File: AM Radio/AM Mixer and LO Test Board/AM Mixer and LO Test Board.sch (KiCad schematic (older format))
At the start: 47 parts, among them J1 RF_IN, J2 IF_FILT_OUT, J3 IF_PREFILT_OUT, J4 RF_IN, Q1 2N2222, Q2 2N2222, Q3 2N2222, T1 SWB2010-1-SM, T2 SWB2010-1-SM, U1 AD711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

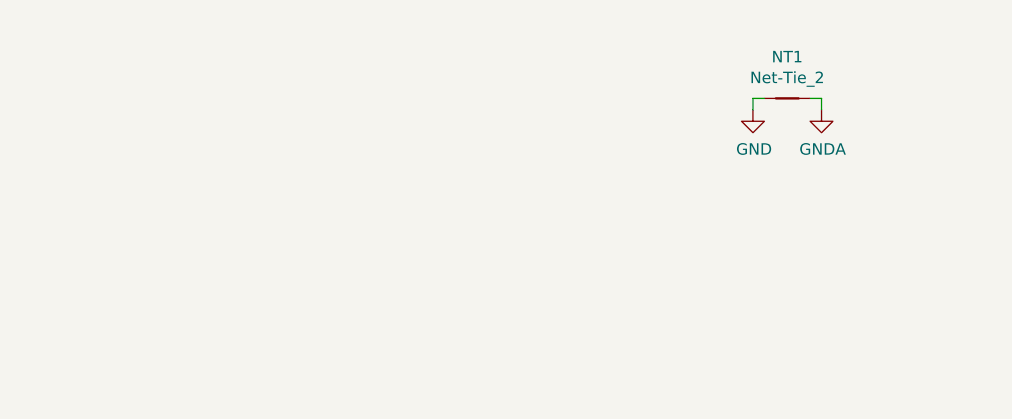
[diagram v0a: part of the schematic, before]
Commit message: Added components to PCB and set up DRC + board outline
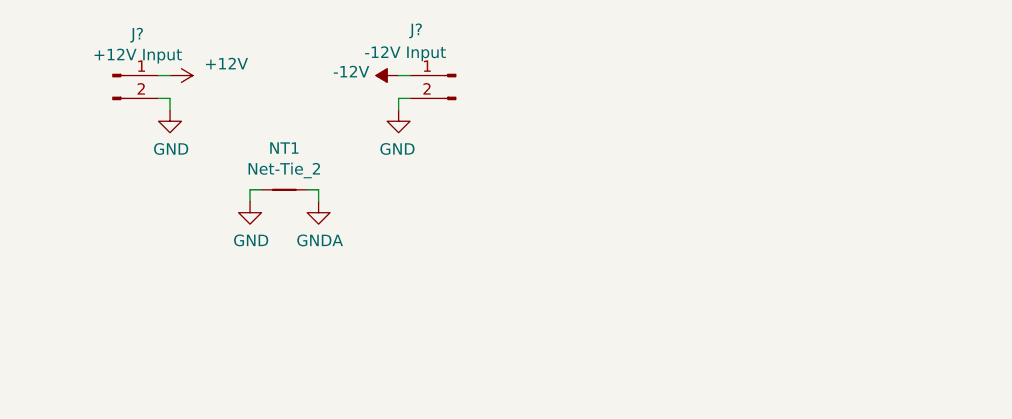
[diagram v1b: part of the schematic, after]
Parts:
- added J?: +12V Input, Connector_PinHeader_2.54mm:PinHeader_1x02_P2.54mm_Vertical, symbol Connector:Conn_01x02_Male
- added J?: -12V Input, Connector_PinHeader_2.54mm:PinHeader_1x02_P2.54mm_Vertical, symbol Connector:Conn_01x02_Male
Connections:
- net +12V: now also J?.1 (Pin_1)
- net -12V: now also J?.1 (Pin_1)
- net GND: now also J?.2 (Pin_2), J?.2 (Pin_2)
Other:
- moved on the sheet: NT1
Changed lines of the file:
@@
 L Device:Net-Tie_2 NT1
 U 1 1 60F78CC0
-P 3900 1100
-F 0 "NT1" H 3900 1281 50  0000 C CNN
-F 1 "Net-Tie_2" H 3900 1190 50  0000 C CNN
-F 2 "NetTie:NetTie-2_SMD_Pad0.5mm" H 3900 1100 50  0001 C CNN
-F 3 "~" H 3900 1100 50  0001 C CNN
-	1    3900 1100
+P 1700 1500
+F 0 "NT1" H 1700 1681 50  0000 C CNN
+F 1 "Net-Tie_2" H 1700 1590 50  0000 C CNN
+F 2 "NetTie:NetTie-2_SMD_Pad0.5mm" H 1700 1500 50  0001 C CNN
+F 3 "~" H 1700 1500 50  0001 C CNN
+	1    1700 1500
 	1    0    0    -1
 $EndComp
@@
 L power:GND #PWR032
 U 1 1 60F79A9F
-P 3750 1150
-F 0 "#PWR032" H 3750 900 50  0001 C CNN
-F 1 "GND" H 3755 977 50  0000 C CNN
-F 2 "" H 3750 1150 50  0001 C CNN
-F 3 "" H 3750 1150 50  0001 C CNN
-	1    3750 1150
+P 1550 1550
+F 0 "#PWR032" H 1550 1300 50  0001 C CNN
+F 1 "GND" H 1555 1377 50  0000 C CNN
+F 2 "" H 1550 1550 50  0001 C CNN
+F 3 "" H 1550 1550 50  0001 C CNN
+	1    1550 1550
 	1    0    0    -1
 $EndComp
 Wire Wire Line
-	3750 1150 3750 1100
+	1550 1550 1550 1500
 Wire Wire Line
-	3750 1100 3800 1100
+	1550 1500 1600 1500
 $Comp
 L power:GNDA #PWR033
 U 1 1 60F81BDB
-P 4050 1150
-F 0 "#PWR033" H 4050 900 50  0001 C CNN
-F 1 "GNDA" H 4055 977 50  0000 C CNN
-F 2 "" H 4050 1150 50  0001 C CNN
-F 3 "" H 4050 1150 50  0001 C CNN
-	1    4050 1150
+P 1850 1550
+F 0 "#PWR033" H 1850 1300 50  0001 C CNN
+F 1 "GNDA" H 1855 1377 50  0000 C CNN
+F 2 "" H 1850 1550 50  0001 C CNN
+F 3 "" H 1850 1550 50  0001 C CNN
+	1    1850 1550
 	1    0    0    -1
 $EndComp
 Wire Wire Line
-	4050 1150 4050 1100
+	1850 1550 1850 1500
 Wire Wire Line
-	4050 1100 4000 1100
+	1850 1500 1800 1500
+$Comp
+L power:+12V #PWR?
+U 1 1 60F9D5C7
+P 1200 1000
+F 0 "#PWR?" H 1200 850 50  0001 C CNN
+F 1 "+12V" V 1150 1150 50  0000 L CNN
+F 2 "" H 1200 1000 50  0001 C CNN
+F 3 "" H 1200 1000 50  0001 C CNN
+	1    1200 1000
+	0    1    1    0
+$EndComp
+Wire Wire Line
+	1150 1000 1200 1000
+$Comp
+L Connector:Conn_01x02_Male J?
+U 1 1 60FA60E9
+P 950 1000
+F 0 "J?" H 1058 1181 50  0000 C CNN
+F 1 "+12V Input" H 1058 1090 50  0000 C CNN
+F 2 "Connector_PinHeader_2.54mm:PinHeader_1x02_P2.54mm_Vertical" H 950 1000 50  0001 C CNN
+F 3 "~" H 950 1000 50  0001 C CNN
+	1    950  1000
+	1    0    0    -1
+$EndComp
+$Comp
+L power:GND #PWR?
+U 1 1 60FA6D03
+P 1200 1150
+F 0 "#PWR?" H 1200 900 50  0001 C CNN
+F 1 "GND" H 1205 977 50  0000 C CNN
+F 2 "" H 1200 1150 50  0001 C CNN
+F 3 "" H 1200 1150 50  0001 C CNN
+	1    1200 1150
+	1    0    0    -1
+$EndComp
+Wire Wire Line
+	1200 1150 1200 1100
+Wire Wire Line
+	1200 1100 1150 1100
+Wire Wire Line
+	2250 1000 2200 1000
+$Comp
+L Connector:Conn_01x02_Male J?
+U 1 1 60FB1804
+P 2450 1000
+F 0 "J?" H 2650 1200 50  0000 R CNN
+F 1 "-12V Input" H 2850 1100 50  0000 R CNN
+F 2 "Connector_PinHeader_2.54mm:PinHeader_1x02_P2.54mm_Vertical" H 2450 1000 50  0001 C CNN
+F 3 "~" H 2450 1000 50  0001 C CNN
+	1    2450 1000
+	-1   0    0    -1
+$EndComp
+$Comp
+L power:GND #PWR?
+U 1 1 60FB180A
+P 2200 1150
+F 0 "#PWR?" H 2200 900 50  0001 C CNN
+F 1 "GND" H 2205 977 50  0000 C CNN
+F 2 "" H 2200 1150 50  0001 C CNN
+F 3 "" H 2200 1150 50  0001 C CNN
+	1    2200 1150
+	-1   0    0    -1
+$EndComp
+Wire Wire Line
+	2200 1150 2200 1100
+Wire Wire Line
+	2200 1100 2250 1100
+$Comp
+L power:-12V #PWR?
+U 1 1 60FB9DF0
+P 2200 1000
+F 0 "#PWR?" H 2200 1100 50  0001 C CNN
+F 1 "-12V" V 2215 1128 50  0000 L CNN
+F 2 "" H 2200 1000 50  0001 C CNN
+F 3 "" H 2200 1000 50  0001 C CNN
+	1    2200 1000
+	0    -1   -1   0
+$EndComp
 $EndSCHEMATC

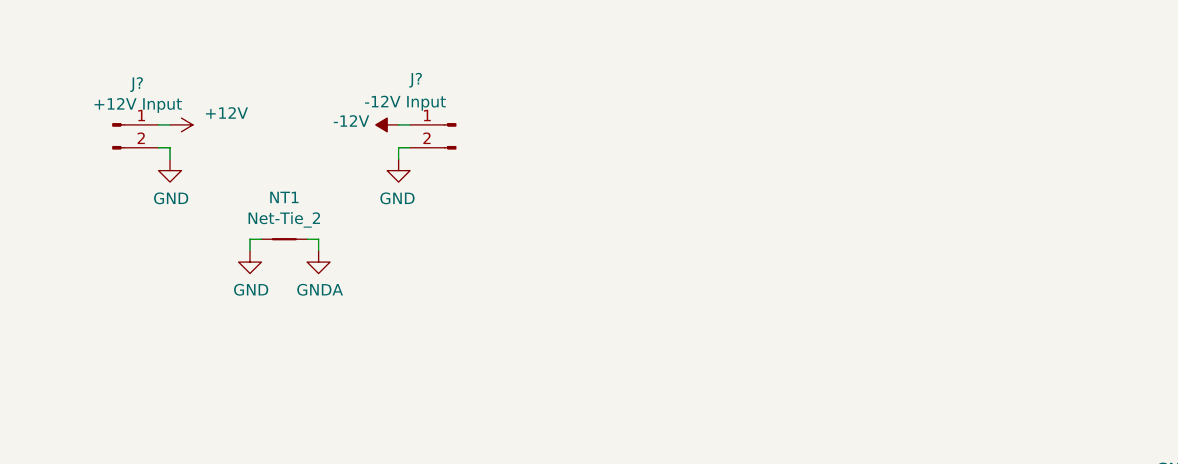
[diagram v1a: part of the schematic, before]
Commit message: Added power regulation, started work on aligning silk screen.
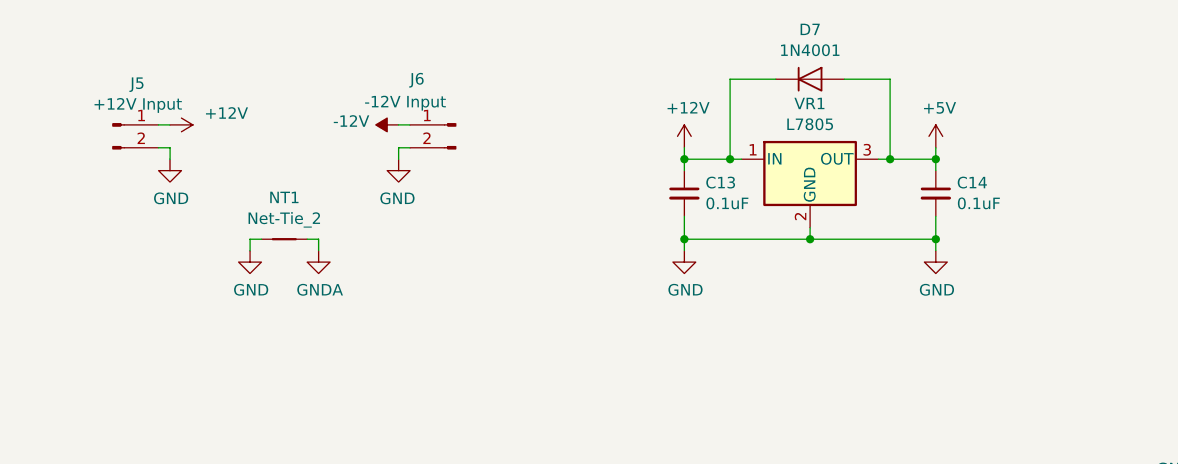
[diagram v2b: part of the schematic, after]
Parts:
- added C13, C14: 0.1uF, Capacitor_SMD:C_0805_2012Metric_Pad1.15x1.40mm_HandSolder, symbol Device:C_Small
- added D7: 1N4001, Diode_THT:D_DO-15_P15.24mm_Horizontal, symbol Device:D
- added VR1: L7805, Package_TO_SOT_THT:TO-220-3_Vertical, symbol Regulator_Linear:L7805
- gave numbers to parts that had none: 2
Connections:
- net +12V: now also C13.1, D7.1 (K), VR1.1 (IN)
- net +5V: now also C14.1, D7.2 (A), VR1.3 (OUT)
- net GND: now also C13.2, C14.2, VR1.2 (GND)
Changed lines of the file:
@@
 	1850 1500 1800 1500
 $Comp
-L power:+12V #PWR?
+L power:+12V #PWR034
 U 1 1 60F9D5C7
 P 1200 1000
-F 0 "#PWR?" H 1200 850 50  0001 C CNN
+F 0 "#PWR034" H 1200 850 50  0001 C CNN
 F 1 "+12V" V 1150 1150 50  0000 L CNN
 F 2 "" H 1200 1000 50  0001 C CNN
@@
 	1150 1000 1200 1000
 $Comp
-L Connector:Conn_01x02_Male J?
+L Connector:Conn_01x02_Male J5
 U 1 1 60FA60E9
 P 950 1000
-F 0 "J?" H 1058 1181 50  0000 C CNN
+F 0 "J5" H 1058 1181 50  0000 C CNN
 F 1 "+12V Input" H 1058 1090 50  0000 C CNN
 F 2 "Connector_PinHeader_2.54mm:PinHeader_1x02_P2.54mm_Vertical" H 950 1000 50  0001 C CNN
@@
 $EndComp
 $Comp
-L power:GND #PWR?
+L power:GND #PWR038
 U 1 1 60FA6D03
 P 1200 1150
-F 0 "#PWR?" H 1200 900 50  0001 C CNN
+F 0 "#PWR038" H 1200 900 50  0001 C CNN
 F 1 "GND" H 1205 977 50  0000 C CNN
 F 2 "" H 1200 1150 50  0001 C CNN
@@
 	2250 1000 2200 1000
 $Comp
-L Connector:Conn_01x02_Male J?
+L Connector:Conn_01x02_Male J6
 U 1 1 60FB1804
 P 2450 1000
-F 0 "J?" H 2650 1200 50  0000 R CNN
+F 0 "J6" H 2650 1200 50  0000 R CNN
 F 1 "-12V Input" H 2850 1100 50  0000 R CNN
 F 2 "Connector_PinHeader_2.54mm:PinHeader_1x02_P2.54mm_Vertical" H 2450 1000 50  0001 C CNN
@@
 $EndComp
 $Comp
-L power:GND #PWR?
+L power:GND #PWR039
 U 1 1 60FB180A
 P 2200 1150
-F 0 "#PWR?" H 2200 900 50  0001 C CNN
+F 0 "#PWR039" H 2200 900 50  0001 C CNN
 F 1 "GND" H 2205 977 50  0000 C CNN
 F 2 "" H 2200 1150 50  0001 C CNN
@@
 	2200 1100 2250 1100
 $Comp
-L power:-12V #PWR?
+L power:-12V #PWR035
 U 1 1 60FB9DF0
 P 2200 1000
-F 0 "#PWR?" H 2200 1100 50  0001 C CNN
+F 0 "#PWR035" H 2200 1100 50  0001 C CNN
 F 1 "-12V" V 2215 1128 50  0000 L CNN
 F 2 "" H 2200 1000 50  0001 C CNN
@@
 	0    -1   -1   0
 $EndComp
+$Comp
+L Regulator_Linear:L7805 VR1
+U 1 1 60DBFF56
+P 4000 1150
+F 0 "VR1" H 4000 1392 50  0000 C CNN
+F 1 "L7805" H 4000 1301 50  0000 C CNN
+F 2 "Package_TO_SOT_THT:TO-220-3_Vertical" H 4025 1000 50  0001 L CIN
+F 3 "http://www.st.com/content/ccc/resource/technical/document/datasheet/41/4f/b3/b0/12/d4/47/88/CD00000444.pdf/files/CD00000444.pdf/jcr:content/translations/en.CD00000444.pdf" H 4000 1100 50  0001 C CNN
+	1    4000 1150
+	1    0    0    -1
+$EndComp
+$Comp
+L Device:C_Small C13
+U 1 1 60DC1760
+P 3450 1300
+F 0 "C13" H 3542 1346 50  0000 L CNN
+F 1 "0.1uF" H 3542 1255 50  0000 L CNN
+F 2 "Capacitor_SMD:C_0805_2012Metric_Pad1.15x1.40mm_HandSolder" H 3450 1300 50  0001 C CNN
+F 3 "~" H 3450 1300 50  0001 C CNN
+	1    3450 1300
+	1    0    0    -1
+$EndComp
+$Comp
+L power:GND #PWR040
+U 1 1 60DC1766
+P 3450 1550
+F 0 "#PWR040" H 3450 1300 50  0001 C CNN
+F 1 "GND" H 3455 1377 50  0000 C CNN
+F 2 "" H 3450 1550 50  0001 C CNN
+F 3 "" H 3450 1550 50  0001 C CNN
+	1    3450 1550
+	1    0    0    -1
+$EndComp
+Wire Wire Line
+	3450 1550 3450 1500
+$Comp
+L Device:C_Small C14
+U 1 1 60DCB43C
+P 4550 1300
+F 0 "C14" H 4642 1346 50  0000 L CNN
+F 1 "0.1uF" H 4642 1255 50  0000 L CNN
+F 2 "Capacitor_SMD:C_0805_2012Metric_Pad1.15x1.40mm_HandSolder" H 4550 1300 50  0001 C CNN
+F 3 "~" H 4550 1300 50  0001 C CNN
+	1    4550 1300
+	1    0    0    -1
+$EndComp
+$Comp
+L power:GND #PWR041
+U 1 1 60DCB442
+P 4550 1550
+F 0 "#PWR041" H 4550 1300 50  0001 C CNN
+F 1 "GND" H 4555 1377 50  0000 C CNN
+F 2 "" H 4550 1550 50  0001 C CNN
+F 3 "" H 4550 1550 50  0001 C CNN
+	1    4550 1550
+	1    0    0    -1
+$EndComp
+Wire Wire Line
+	4550 1550 4550 1500
+Wire Wire Line
+	3450 1200 3450 1150
+Wire Wire Line
+	3450 1150 3650 1150
+Wire Wire Line
+	4550 1200 4550 1150
+Wire Wire Line
+	4550 1150 4350 1150
+$Comp
+L Device:D D7
+U 1 1 60DE6E61
+P 4000 800
+F 0 "D7" H 4000 1016 50  0000 C CNN
+F 1 "1N4001" H 4000 925 50  0000 C CNN
+F 2 "Diode_THT:D_DO-15_P15.24mm_Horizontal" H 4000 800 50  0001 C CNN
+F 3 "~" H 4000 800 50  0001 C CNN
+	1    4000 800
+	1    0    0    -1
+$EndComp
+Wire Wire Line
+	3650 1150 3650 800
+Wire Wire Line
+	3650 800  3850 800
+Connection ~ 3650 1150
+Wire Wire Line
+	3650 1150 3700 1150
+Wire Wire Line
+	4150 800  4350 800
+Wire Wire Line
+	4350 800  4350 1150
+Connection ~ 4350 1150
+Wire Wire Line
+	4350 1150 4300 1150
+$Comp
+L power:+12V #PWR036
+U 1 1 60DFAFFF
+P 3450 1100
+F 0 "#PWR036" H 3450 950 50  0001 C CNN
+F 1 "+12V" H 3465 1273 50  0000 C CNN
+F 2 "" H 3450 1100 50  0001 C CNN
+F 3 "" H 3450 1100 50  0001 C CNN
+	1    3450 1100
+	1    0    0    -1
+$EndComp
+Wire Wire Line
+	3450 1100 3450 1150
+Connection ~ 3450 1150
+$Comp
+L power:+5V #PWR037
+U 1 1 60E05B0B
+P 4550 1100
+F 0 "#PWR037" H 4550 950 50  0001 C CNN
+F 1 "+5V" H 4565 1273 50  0000 C CNN
+F 2 "" H 4550 1100 50  0001 C CNN
+F 3 "" H 4550 1100 50  0001 C CNN
+	1    4550 1100
+	1    0    0    -1
+$EndComp
+Wire Wire Line
+	4550 1100 4550 1150
+Connection ~ 4550 1150
+Wire Wire Line
+	3450 1500 4000 1500
+Wire Wire Line
+	4000 1500 4000 1450
+Connection ~ 3450 1500
+Wire Wire Line
+	3450 1500 3450 1400
+Wire Wire Line
+	4000 1500 4550 1500
+Connection ~ 4000 1500
+Connection ~ 4550 1500
+Wire Wire Line
+	4550 1500 4550 1400
 $EndSCHEMATC
